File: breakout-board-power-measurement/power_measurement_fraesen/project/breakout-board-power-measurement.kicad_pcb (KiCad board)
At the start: 2 copper layers, 70.6 x 40.2 mm, 83 parts, among them J1 Screw_Terminal_01x04, J2 Conn_01x09, J3 Conn_01x07, J4 Conn_01x02, U1 MCP3911A0-E-SS, U2 Si8641BA-B-IU, U3 LM317_TO-252, Y1 10M

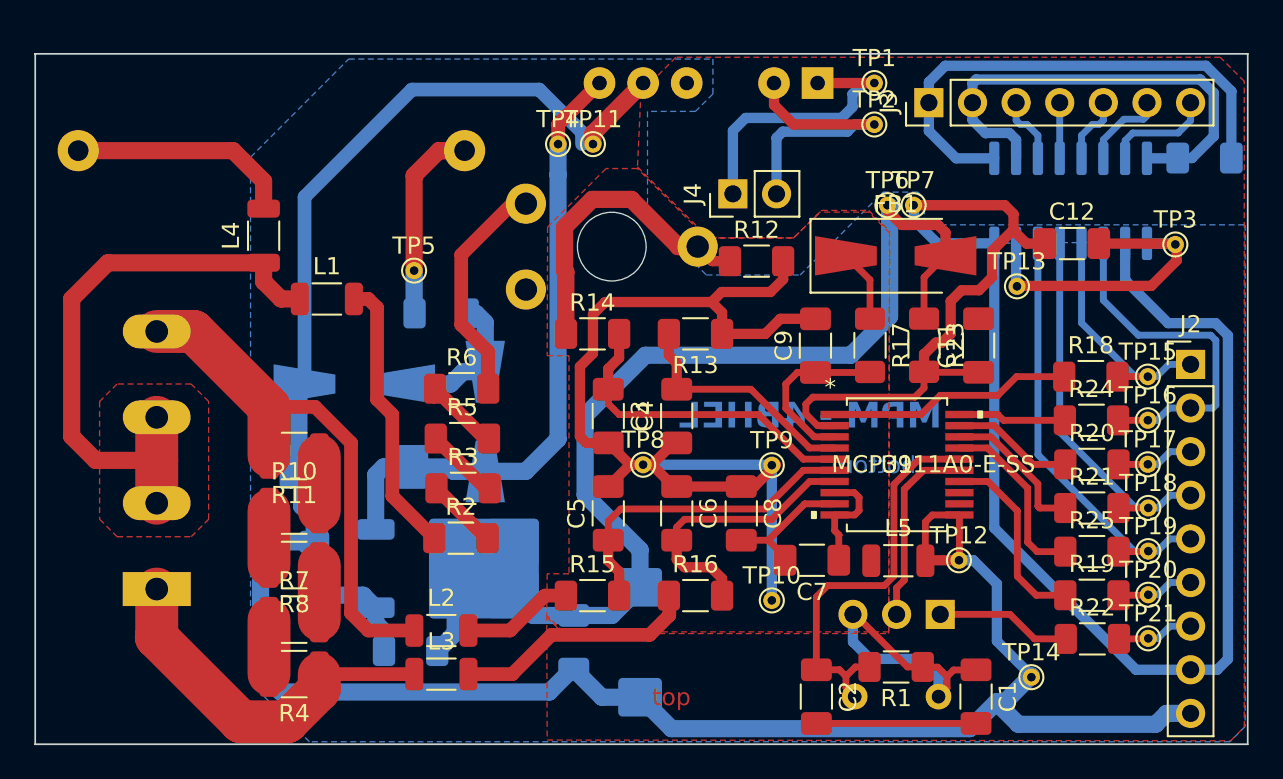
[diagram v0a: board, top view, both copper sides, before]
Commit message: power measurement fertig fürs fräsen
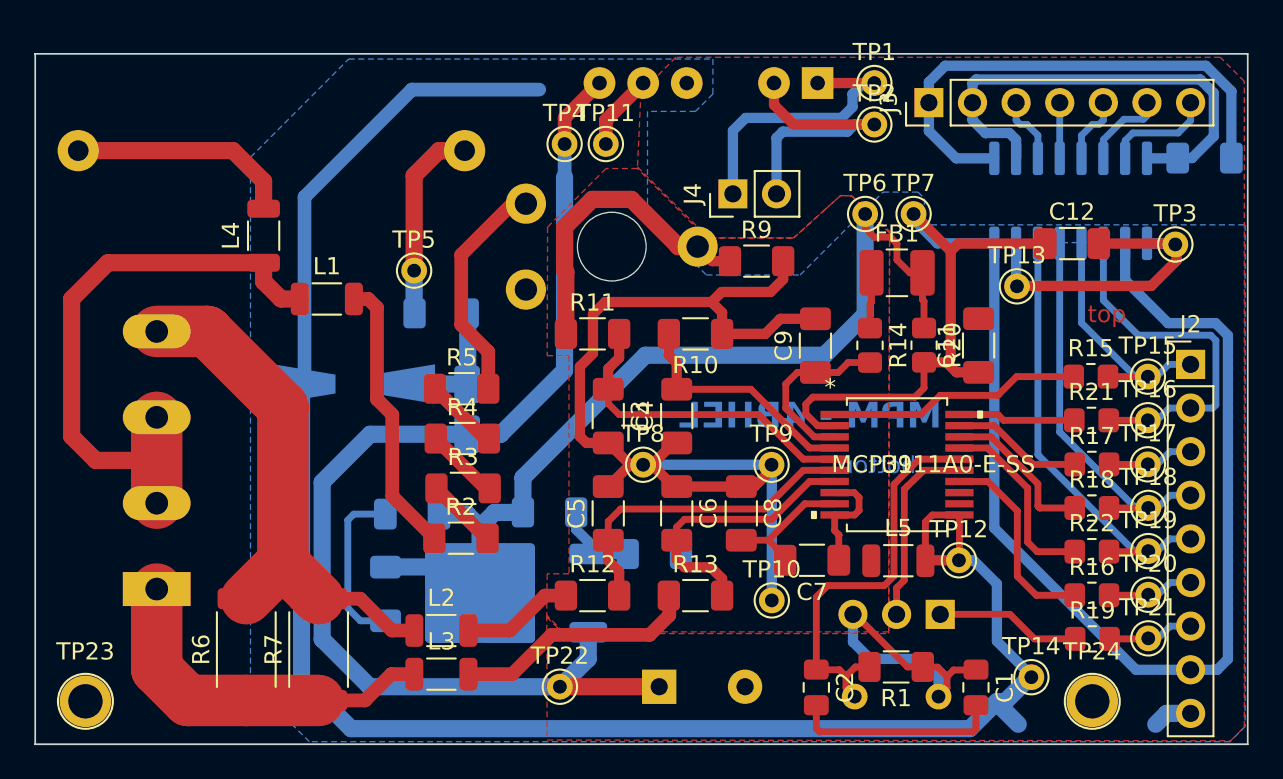
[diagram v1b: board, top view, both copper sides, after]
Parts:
- removed the R10 at (133.5, 139.2)
- removed the R11 at (133.5, 136.0)
- removed the R4 at (133.5, 148.7)
- removed the R8 at (133.5, 142.4)
- added R6: 50m, Resistor_SMD:R_2512_6332Metric, F.Cu at (130.7, 147.3)
- added TP22: TestPoint, Via:Via_THTPad_D1.5mm_Drill0.8mm, F.Cu at (148.9, 149.4)
- added TP23: TestPoint, Screwhole:Screwhole_THTPad_D3.0mm_Drill2.0mm, F.Cu at (121.3, 150.3)
- added TP24: TestPoint, Screwhole:Screwhole_THTPad_D3.0mm_Drill2.0mm, F.Cu at (179.9, 150.3)
- C1, C2: value 22p -> 18p; footprint Capacitor_SMD:C_1206_3216Metric_Pad1.33x1.80mm_HandSolder -> Capacitor_SMD:C_0805_2012Metric_Pad1.18x1.45mm_HandSolder
- C10: value 470n/530 -> 820n/530
- C13: footprint Capacitor_Tantalum_SMD:CP_EIA-7343-31_Kemet-D_Pad2.25x2.55mm_HandSolder -> Capacitor_THT:CP_Radial_D10.0mm_P5.00mm
- C15: value 10u/50 -> 10u; footprint Capacitor_Tantalum_SMD:CP_EIA-7343-31_Kemet-D_Pad2.25x2.55mm_HandSolder -> Capacitor_SMD:C_1206_3216Metric_Pad1.33x1.80mm_HandSolder
- D2: footprint Diode_SMD:D_SMA-SMB_Universal_Handsoldering -> Diode_SMD:D_MicroMELF_Handsoldering
- FB1: footprint Diode_SMD:D_SMA-SMB_Universal_Handsoldering -> Inductor_SMD:L_1210_3225Metric_Pad1.42x2.65mm_HandSolder
- R1: value 1M -> 1.2M
- R14: renamed from R17; footprint Resistor_SMD:R_1206_3216Metric_Pad1.30x1.75mm_HandSolder -> Resistor_SMD:R_0805_2012Metric_Pad1.20x1.40mm_HandSolder
- R15: renamed from R18; footprint Resistor_SMD:R_1206_3216Metric_Pad1.30x1.75mm_HandSolder -> Resistor_SMD:R_0805_2012Metric_Pad1.20x1.40mm_HandSolder
- R16: renamed from R19; footprint Resistor_SMD:R_1206_3216Metric_Pad1.30x1.75mm_HandSolder -> Resistor_SMD:R_0805_2012Metric_Pad1.20x1.40mm_HandSolder
- R17: renamed from R20; footprint Resistor_SMD:R_1206_3216Metric_Pad1.30x1.75mm_HandSolder -> Resistor_SMD:R_0805_2012Metric_Pad1.20x1.40mm_HandSolder
- R18: renamed from R21; footprint Resistor_SMD:R_1206_3216Metric_Pad1.30x1.75mm_HandSolder -> Resistor_SMD:R_0805_2012Metric_Pad1.20x1.40mm_HandSolder
- R19: renamed from R22; footprint Resistor_SMD:R_1206_3216Metric_Pad1.30x1.75mm_HandSolder -> Resistor_SMD:R_0805_2012Metric_Pad1.20x1.40mm_HandSolder
- R20: renamed from R23; footprint Resistor_SMD:R_1206_3216Metric_Pad1.30x1.75mm_HandSolder -> Resistor_SMD:R_0805_2012Metric_Pad1.20x1.40mm_HandSolder
- R21: renamed from R24; footprint Resistor_SMD:R_1206_3216Metric_Pad1.30x1.75mm_HandSolder -> Resistor_SMD:R_0805_2012Metric_Pad1.20x1.40mm_HandSolder
- R22: renamed from R25; footprint Resistor_SMD:R_1206_3216Metric_Pad1.30x1.75mm_HandSolder -> Resistor_SMD:R_0805_2012Metric_Pad1.20x1.40mm_HandSolder
- R24: renamed from R27; value 1k6 -> 1k5
- R25: renamed from R28; value 1k -> 910
- R7: footprint Resistor_SMD:R_1210_3225Metric -> Resistor_SMD:R_2512_6332Metric
- TP1, TP10, TP11, TP12, TP13, TP14, TP15, TP16, TP17, TP18, TP19, TP2, TP20, TP21, TP3, TP4, TP5, TP6, TP7, TP8, TP9: footprint TestPoint:TestPoint_THTPad_D1.0mm_Drill0.5mm -> Via:Via_THTPad_D1.5mm_Drill0.8mm
- moved C13 21.9 mm to (154.7, 149.4), turned to 0 degrees
- moved R24 19.8 mm to (154.4, 141.7), turned to 0 degrees
- moved C15 15.2 mm to (140.3, 139.4), turned to 180 degrees
- moved R25 11.4 mm to (148.3, 139.3), turned to 0 degrees
- moved C14 11.3 mm to (138.8, 144.1)
- moved U3 2.70 mm to (145.6, 144.0), turned to 180 degrees
- moved R7 2.25 mm to (134.9, 147.3), turned to 90 degrees
- moved TP6 1.39 mm to (166.7, 121.9)
- moved D2 1.27 mm to (143.6, 133.3)
- moved FB1 0.99 mm to (168.6, 125.3)
- moved TP11 0.75 mm to (151.6, 117.8)
- moved C1 0.54 mm to (173.2, 149.5)
- moved C2 0.54 mm to (163.9, 149.5)
- moved TP7 0.51 mm to (169.5, 121.9)
- moved TP4 0.38 mm to (149.2, 117.8)
- renumbered R13 to R10, R14 to R11, R15 to R12, R16 to R13, R26 to R23, R5 to R4, R6 to R5, R9 to R8, R12 to R9
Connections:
- R7 pad 1: Net-(R4-Pad2) (its old number) -> /current_neg
- R7 pad 2: Net-(R7-Pad2) -> /current_pos
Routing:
- net /LM317_Vin: track 36.2 -> 68.2 mm
- net GNDD: track 163.5 -> 158.2 mm
- net /3V3D: track 102.5 -> 97.4 mm
- net +3.3V: track 59.9 -> 54.9 mm
- net Net-(R7-Pad2): track 3.18 -> 0.00 mm
- net Net-(R4-Pad2) (its old number): track 3.18 -> 0.00 mm
- net Net-(R10-Pad2): track 3.18 -> 0.00 mm
- net Net-(R10-Pad1): track 3.17 -> 0.00 mm
- net Net-(U3-ADJ): track 6.60 -> 5.01 mm
- net Net-(D1-K): track 9.12 -> 7.83 mm
- removed copper zone on F.Cu, net HIGH_in
